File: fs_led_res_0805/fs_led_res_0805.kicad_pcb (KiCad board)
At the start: 2 copper layers, 14 x 4 mm, 4 parts

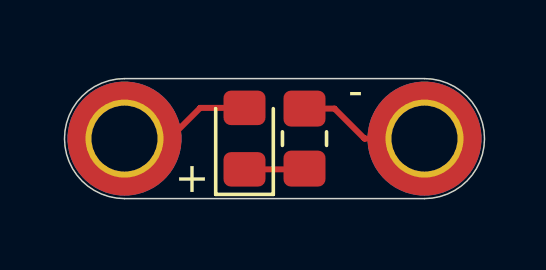
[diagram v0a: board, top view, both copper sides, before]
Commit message: update fs_led_res_0805 board revision and export single-unit gerbers
Board/schematic edits since the last panel order. manufacture/jlc/ was
still holding the mismatched resistor_0805_order gerbers (same issue as
fs_led_res_0603); replaced with a fresh export straight from
fs_led_res_0805.kicad_pcb, since this board is now ordered as a single
unit rather than the 1008-up manufacture/led_res_0805_order.kicad_pcb
panel.

Co-Authored-By: Claude Sonnet 5 <noreply@anthropic.com>
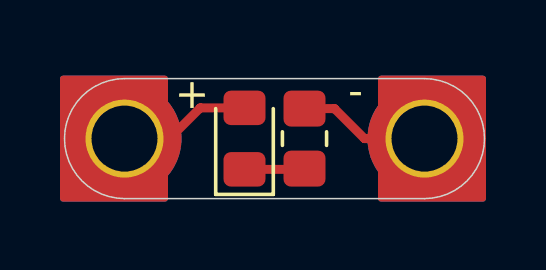
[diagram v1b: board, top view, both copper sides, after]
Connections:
- net Net-(D1-A) renamed VCC
- net Net-(H2-Pad1) renamed GND
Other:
- board text added: "@borisnotes"
- board text removed: "@flicker stitch"
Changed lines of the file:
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@@
 			(outputformat 1)
 			(mirror no)
-			(drillshape 1)
+			(drillshape 0)
 			(scaleselection 1)
-			(outputdirectory "")
+			(outputdirectory "gerbers/")
 		)
 	)
@@
 			(layers "F.Cu" "F.Mask" "F.Paste")
 			(roundrect_rratio 0.208333)
-			(net "Net-(H2-Pad1)")
+			(net "GND")
 			(pintype "passive")
 		)
@@
 			(at 0 2.85 0)
 			(layer "F.Fab")
+			(hide yes)
 			(effects
 				(font
@@
 			(layers "*.Cu" "*.Mask")
 			(remove_unused_layers no)
-			(net "Net-(H2-Pad1)")
+			(net "GND")
 			(pinfunction "1_1")
 			(pintype "input")
@@
 			(size 3.8 3.8)
 			(layers "F.Cu" "F.Mask")
-			(net "Net-(H2-Pad1)")
+			(net "GND")
 			(pinfunction "1_1")
 			(pintype "input")
@@
 			(size 3.8 3.8)
 			(layers "B.Cu" "B.Mask")
-			(net "Net-(H2-Pad1)")
+			(net "GND")
 			(pinfunction "1_1")
 			(pintype "input")
@@
 			(layers "F.Cu" "F.Mask" "F.Paste")
 			(roundrect_rratio 0.217391)
-			(net "Net-(D1-A)")
+			(net "VCC")
 			(pinfunction "A_2")
 			(pintype "passive")
@@
 			(at 0 2.85 0)
 			(layer "F.Fab")
+			(hide yes)
 			(effects
 				(font
@@
 			(layers "*.Cu" "*.Mask")
 			(remove_unused_layers no)
-			(net "Net-(D1-A)")
+			(net "VCC")
 			(pinfunction "1_1")
 			(pintype "input")
@@
 			(size 3.8 3.8)
 			(layers "F.Cu" "F.Mask")
-			(net "Net-(D1-A)")
+			(net "VCC")
 			(pinfunction "1_1")
 			(pintype "input")
@@
 			(size 3.8 3.8)
 			(layers "B.Cu" "B.Mask")
-			(net "Net-(D1-A)")
+			(net "VCC")
 			(pinfunction "1_1")
 			(pintype "input")
@@
 		)
 		(embedded_fonts no)
+	)
+	(gr_rect
+		(start 137.95 78)
+		(end 141.35 82)
+		(stroke
+			(width 0.2)
+			(type solid)
+		)
+		(fill yes)
+		(layer "F.Cu")
+		(net "VCC")
+	)
+	(gr_rect
+		(start 148.55 78)
+		(end 151.95 82)
+		(stroke
+			(width 0.2)
+			(type solid)
+		)
+		(fill yes)
+		(layer "F.Cu")
+		(net "GND")
+	)
+	(gr_rect
+		(start 137.95 78)
+		(end 141.35 82)
+		(stroke
+			(width 0.2)
+			(type solid)
+		)
+		(fill yes)
+		(layer "F.Mask")
+	)
+	(gr_rect
+		(start 148.55 78)
+		(end 151.95 82)
+		(stroke
+			(width 0.2)
+			(type solid)
+		)
+		(fill yes)
+		(layer "F.Mask")
+	)
+	(gr_rect
+		(start 137.95 78)
+		(end 141.35 82)
+		(stroke
+			(width 0.2)
+			(type solid)
+		)
+		(fill yes)
+		(layer "B.Cu")
+		(net "VCC")
+	)
+	(gr_rect
+		(start 148.55 78)
+		(end 151.95 82)
+		(stroke
+			(width 0.2)
+			(type solid)
+		)
+		(fill yes)
+		(layer "B.Cu")
+		(net "GND")
+	)
+	(gr_rect
+		(start 137.95 78)
+		(end 141.35 82)
+		(stroke
+			(width 0.2)
+			(type solid)
+		)
+		(fill yes)
+		(layer "B.Mask")
+	)
+	(gr_rect
+		(start 148.55 78)
+		(end 151.95 82)
+		(stroke
+			(width 0.2)
+			(type solid)
+		)
+		(fill yes)
+		(layer "B.Mask")
 	)
 	(gr_line
@@
 	)
 	(gr_text "+"
-		(at 142.25 81.9 0)
+		(at 142.25 79.1 0)
 		(layer "F.SilkS")
 		(effects
@@
 		)
 	)
-	(gr_text "@flicker\nstitch"
-		(at 145 82 0)
+	(gr_text "@borisnotes"
+		(at 145.15 80.35 25)
 		(layer "B.SilkS")
 		(effects
 			(font
-				(size 0.9 0.9)
+				(size 0.9 0.85)
 			)
 			(justify bottom mirror)
@@
 	)
 	(gr_text "0805"
-		(at 145 79.3 0)
+		(at 146.35 81.9 0)
 		(layer "B.SilkS")
 		(effects
@@
 	)
 	(segment
+		(start 145.975 81.025)
+		(end 146 81)
+		(width 0.2)
+		(layer "F.Cu")
+		(net "Net-(D1-K)")
+	)
+	(segment
+		(start 144 81.025)
+		(end 145.975 81.025)
+		(width 0.3)
+		(layer "F.Cu")
+		(net "Net-(D1-K)")
+	)
+	(segment
 		(start 141.5 80)
 		(end 142.525 78.975)
-		(width 0.2)
-		(layer "F.Cu")
-		(net "Net-(D1-A)")
+		(width 0.3)
+		(layer "F.Cu")
+		(net "VCC")
 	)
 	(segment
 		(start 140 80)
 		(end 141.5 80)
-		(width 0.2)
-		(layer "F.Cu")
-		(net "Net-(D1-A)")
+		(width 0.3)
+		(layer "F.Cu")
+		(net "VCC")
 	)
 	(segment
 		(start 142.525 78.975)
 		(end 144 78.975)
-		(width 0.2)
-		(layer "F.Cu")
-		(net "Net-(D1-A)")
-	)
-	(segment
-		(start 145.975 81.025)
-		(end 146 81)
-		(width 0.2)
-		(layer "F.Cu")
-		(net "Net-(D1-K)")
-	)
-	(segment
-		(start 144 81.025)
-		(end 145.975 81.025)
-		(width 0.2)
-		(layer "F.Cu")
-		(net "Net-(D1-K)")
+		(width 0.3)
+		(layer "F.Cu")
+		(net "VCC")
 	)
 	(segment
 		(start 148 80)
 		(end 150 80)
-		(width 0.2)
-		(layer "F.Cu")
-		(net "Net-(H2-Pad1)")
+		(width 0.3)
+		(layer "F.Cu")
+		(net "GND")
 	)
 	(segment
 		(start 147 79)
 		(end 148 80)
-		(width 0.2)
-		(layer "F.Cu")
-		(net "Net-(H2-Pad1)")
+		(width 0.3)
+		(layer "F.Cu")
+		(net "GND")
 	)
 	(segment
 		(start 146 79)
 		(end 147 79)
-		(width 0.2)
-		(layer "F.Cu")
-		(net "Net-(H2-Pad1)")
+		(width 0.3)
+		(layer "F.Cu")
+		(net "GND")
 	)
 	(embedded_fonts no)
